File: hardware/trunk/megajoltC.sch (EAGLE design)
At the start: 92 parts, among them IC2 MCP1826, IC9 74AC240, U3 MAX9924, U4 ZXMS6004FF, U5 MAX9924, U6 ZXMS6004FF, U7 MCP1700, U8 FAN8303, X1 MINI_USB_SHIELD, X2 MOLEX_MINIFIT-22

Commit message: Schematic V1 for MJ2/C
Also added pinmux for xmc4200.  Board is partially routed to assist in pinout
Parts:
- removed C28: 1nF, rcl:C-USC0603
- removed C29: .001uf, rcl:C-USC0603
- removed C33: 10nF, rcl:C-USC0603
- removed C34: 0.1uF, rcl:C-USC0603
- removed C35: 1uF, rcl:C-USC0603
- removed C44: 0.22uf, rcl:C-USC0603
- removed C45: .1uf, rcl:C-USC0603
- removed C46: 10uF, rcl:CPOL-USSMCA
- removed C49: 0.1uf, rcl:C-USC0603
- removed D10, D11, D2, D3, D4, D5, D8, D9: schottky, smt_diodes:ZENER2
- removed IC9: 74AC240, 74xx-eu:74S240DW
- removed POWER, S1, S2: PANEL_LED, LEDs:PANEL_LED
- removed R21, R24, R25: 1K, rcl:R-US_R0603
- removed R33: 20K 1%, rcl:R-US_R0603
- removed R34: 39K 1%, rcl:R-US_R0603
- removed R37: 51K 1%, rcl:R-US_R0603
- removed R38: 10K 1%, rcl:R-US_R0603
- removed SV2: (no value), con-lsta:FE08-1
- removed U3, U5: MAX9924, max9924_9927:MAX9924
- removed U6: ZXMS6004FF, power_mosfets:ZXMS6004FF
- removed U7: MCP1700, mcp1700:MCP1700
- removed X2: MOLEX_MINIFIT-22, molex_mini-fit:MOLEX_MINIFIT-22
- added C10, C12: 10uF, resistor:C-USC0603
- added C11: 0.1uf, rcl:C-USC0603
- added C13, C15, C16, C17, C18, C19, C7, C8: 100nF, resistor:C-USC0603
- added C25, C26: 33pF, SparkFun:CAP0603
- added C3, C4: 47pF, resistor:C-USC0603
- added C48: 0.1uF, rcl:C-USC0805
- added C5: 100nf, resistor:C-USC0603
- added C6, C9: 4.7uF, resistor:C-USC0603
- added CN2: CAP_ARRAY_41206_ARRAY, cap_array:CAP_ARRAY_41206_ARRAY
- added IC1: IC_FT230X-SSOP-16, dp_devices:IC_FT230X-SSOP-16
- added IC3: MCP1826, linear:LM340S
- added J3: JUMPER_CLOSEDTHICK, jumpers:JUMPER_CLOSEDTHICK
- added L1: 1uH, smt_inductors:INDUCTOR
- added R1, R3: 27, resistor:R-US_R0603
- added R31: 100, resistor:R-US_R0603
- added R39: 1k, resistor:R-US_R0603
- added R4: 4.7k, resistor:R-US_R0603
- added R40, R41, R42: 100, rcl:R-US_R0603
- added R43, R44, R45, R46, R47: 1K, rcl:R-US_R0603
- added R5, R6: 10k, resistor:R-US_R0603
- added RN1: 5.6K, resistor-dil:4R-N0603-ARC
- added RN2: 10K, resistor-dil:4R-N0603-ARC
- added T2, T3: (no value), transistor:-NPN-SOT23-EBC
- added TC2: TC2050-IDC-NL, TagConnect:TC2050-IDC-NL
- added TLV271: TLV271, texas_instruments:TLV271
- added U$1: INF-PG-VQFN-48-53-5200X5200TE5, infineon_xmc:INF-PG-VQFN-48-53-5200X5200TE5
- added U$2: ESP8266_ESP-12, ESP8266-ESP12:ESP8266_ESP-12
- added U$3, U$7, U12: PESDXS4UD, smt_diodes:PESDXS4UD
- added U$4: 74AC240, dp_devices:74AC240
- added U$5: MAX9926, max9924_9927:MAX9926
- added U$6: TRIPLE_PANEL_LED, LEDs:TRIPLE_PANEL_LED
- added U1: MCP1700, mcp1700:MCP1700
- added U11: TLV274, op_amps:TLV274SO14
- added U18: MCP2551SO8, can:MCP2551SO8
- added X3: MOLEX_MINIFIT-22, molex_mini-fit:MOLEX_MINIFIT-22
- added XTAL1: 8MHz, SparkFun2:CRYSTAL5X3
- C20: value 1nF -> 10uF; device rcl:C-USC0603 -> rcl:CPOL-USSMCA
- C21: value .001uF -> 0.1uF; device rcl:C-USC0603 -> rcl:C-USC0603K
- C22: value 0.22uF -> 10nF
- C23: value 10nF -> 10uF; device rcl:C-USC0603 -> rcl:CPOL-USSMCA
- C24: value 0.1uF -> 10uF; device rcl:C-USC0603 -> rcl:CPOL-USSMCA
- C27: value 1uF -> .1uf; device rcl:C-USC0603 -> resistor:C-USC0603
- C30: value 0.22uf -> 0.1uF
- C31: value .001uf -> 1uF
- C32: value 0.22uf -> 1nF
- C43: value .001uf -> 1nF
- R10, R9: value 10K -> 100k; device rcl:R-US_R0603 -> resistor:R-US_R0603
- R11, R29, R30: value 100 -> 1K
- R12, R16, R19, R20: value 1K -> 10K; device rcl:R-US_R0603 -> rcl:R-US_R1206
- R14, R17: value 20K 1% -> 10K
- R15, R18: value 39K 1% -> 10K
- R22: value 1K -> 2.1k; device rcl:R-US_R0603 -> resistor:R-US_R0603
- R23: value 1K -> 10K
- R27: value 18K 1% -> 24K 1%
- R28: value 2.43K 1% -> 2.94K 1%
- R7: value 2.2K -> 120
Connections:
- removed net +12V: L2.2, R13.2, R25.2, R36.2, X2.P2
- removed net +6V: C2.+, IC2.IN
- removed net ADC0: C45.1, R37.2, R38.1
- removed net ADC4: C30.1, D8.A, D9.C, R14.2, R15.2
- removed net ADC5: C32.1, D10.A, D11.C, R17.2, R18.2
- removed net ADC6: C36.1, R32.2
- removed net ADC7: C44.1, D4.C, D5.A, R33.2, R34.2
- removed net AUX_IN: C29.1, R14.1, X2.P6
- removed net GPI0: D2.A, D3.C
- removed net GPO0: IC9B.A1
- removed net GPO1: IC9A.A4
- removed net GPO10: IC9A.G, IC9B.G
- removed net GPO11: U4.G
- removed net GPO2: IC9B.A2
- removed net GPO3: IC9A.A3
- removed net GPO4: IC9B.A3
- removed net GPO5: IC9A.A2
- removed net GPO6: IC9B.A4
- removed net GPO7: IC9A.A1
- removed net GPO8: R35.1
- removed net GPO9: U6.G
- removed net N$14: C20.2, R8.1, U5.IN-
- removed net N$19: R11.2, S1.A
- removed net N$6: C28.2, R10.1, U3.IN-
- removed net OPTION_IN: C21.1, R7.1, X2.P7
- removed net PROC_PULSE_IN: C22.1, R7.2
- removed net RESET: SV2.2
- removed net SAFE12V: C41.+, D6.C, D7.C, R37.1, U8.VIN
- removed net SHIFT_LIGHT: R25.1, U6.D1, X2.P20
- removed net TCK: SV2.5
- removed net TDI: SV2.3
- removed net TDO: SV2.6
- removed net TEMP_IN: C43.1, R33.1, X2.P4
- removed net TIMER0: U5.COUT
- removed net TIMER1: U3.COUT
- removed net TMS: SV2.4
- removed net V+: C46.+, SV2.1, U7.VOUT
- new net +3V3: C12.1, C13.1, C15.1, C16.1, C17.1, C18.1, C19.1, C20.+, C6.1, C7.1, C8.1, C9.1, IC1.VCC, R31.2, R6.2, R9.1, TC2.1, U$1.VBAT, U$1.VDDA, U$1.VDDC1, U$1.VDDC2, U$1.VDDP1, U$1.VDDP2, U$1.VDDP3, U$2.VCC, U1.VOUT
- new net AGND: C13.2, C27.2, C48.2, CN2A.1, CN2B.1, CN2D.1, J3.1, R22.1, RN2A.1, RN2B.1, RN2C.1, TLV271.GND, U$1.VSSA, U11G$5.V-, U12.2, U12.5
- new net ANALOG-FREQ_1_OPAMP_OUT1: RN1C.2, U11G$1.-IN, U11G$1.OUT
- new net ANALOG-FREQ_1_OPAMP_OUT2: RN1B.2, U11G$2.-IN, U11G$2.OUT
- new net ANALOG-FREQ_1_OPAMP_OUT3: RN1A.2, U11G$3.-IN, U11G$3.OUT
- new net ANALOG-FREQ_1_OPAMP_OUT4: RN1D.1, TLV271.IN-, TLV271.OUT
- new net CAM_TIM_IN: U$1.P2.4, U$5.COUT2
- new net CANH: R7.1, U18G$1.CANH, X3.P21
- new net CANL: R7.2, U18G$1.CANL, X3.P2
- new net CAN_RX: U$1.P14.3, U18G$1.RXD
- new net CAN_TX: U$1.P2.0, U18G$1.TXD
- new net CLT_ADC: RN1C.1, RN2C.2, U$1.P14.0
- new net CLT_IN: R12.2, X3.P11
- new net CRANK_TIM_IN: U$1.P1.3, U$5.COUT1
- new net ESP_GPIO0: U$2.GPIO0
- new net ESP_RXD: U$1.P2.5, U$2.RXD
- new net ESP_TXD: U$1.P2.2, U$2.TXD
- new net FTDI_DM: C3.1, R1.1, X1G$1.2
- new net FTDI_DP: C4.1, R3.1, X1G$1.3
- new net FTDI_RXD: IC1.RXD, U$1.P1.5
- new net FTDI_TXD: IC1.TXD, U$1.P1.4
- new net FTDI_VBUS_SENSE: IC1.CBUS0, R4.1, R5.2
- new net GPO_COIL1: U$1.P0.0, U$4G$1.A1
- new net GPO_COIL2: U$1.P0.1, U$4G$1.A2
- new net GPO_COIL3: U$1.P0.2, U$4G$1.A3
- new net GPO_COIL4: U$1.P0.3, U$4G$1.A4
- new net GPO_COIL5: U$1.P0.4, U$4G$2.A1
- new net GPO_COIL6: U$1.P0.5, U$4G$2.A2
- new net GPO_COIL7: U$1.P0.6, U$4G$2.A3
- new net GPO_COIL8: U$1.P0.7, U$4G$2.A4
- new net GPO_COIL_EN: U$1.P0.8, U$4G$1.G, U$4G$2.G
- new net IAT_ADC: RN1A.1, RN2A.2, U$1.P14.4
- new net IAT_IN: R19.2, X3.P12
- new net MAP_ADC: C36.1, R32.2, U$1.P14.7
- new net MAX_DIRN: R14.1, U$5.DIRN
- new net N$1: IC1.USB+, R3.2
- new net N$17: C10.1, R6.1, U$2.REST
- new net N$18: R31.1, U$2.CH_PD
- new net N$20: R40.2, U$6G$1.A
- new net N$23: R42.2, U$6G$3.A
- new net N$24: R39.2, U$2.GPIO15
- new net N$25: C25.2, U$1.XTAL1, XTAL1.2
- new net N$36: R11.1, U$3.6, U$4G$1.Y1
- new net N$37: R29.1, U$3.4, U$4G$1.Y2
- new net N$38: R30.1, U$3.3, U$4G$1.Y3
- new net N$39: R43.1, U$3.1, U$4G$1.Y4
- new net N$4: C5.1, IC1.!RESET, IC1.3V3OUT, IC1.VCCIO
- new net N$40: R44.1, U$4G$2.Y1, U$7.6
- new net N$41: R45.1, U$4G$2.Y2, U$7.4
- new net N$42: R46.1, U$4G$2.Y3, U$7.3
- new net N$43: R47.1, U$4G$2.Y4, U$7.1
- new net N$56: C23.+, IC3.OUT, L1.1
- new net PGM_GPO: U$1.P2.3, U4.G
- new net RAW_+12V: L2.2, X3.P22
- new net SAFE_+12V: C27.1, C41.+, D6.C, D7.C, R13.2, R20.2, R36.2, TLV271.VDD, U8.VIN
- new net STATUS_LED_1: R2.2, U$1.P14.8
- new net STATUS_LED_2: R8.2, U$1.P14.9
- new net SWCLK: R10.2, TC2.4, U$1.TCK/SWCLK
- new net SWDIO: R9.2, TC2.2, U$1.TMS/SWDIO
- new net TACH_GPO: R35.1, U$1.P2.1
- new net TPS_ADC: RN1B.1, RN2B.2, U$1.P14.5
- new net VBATT_ADC: R22.2, RN1D.2, U$1.P14.6
- new net VDD: C2.+, C24.+, C39.+, IC2.IN, IC3.IN, L3.1, R27.1, U1.VIN
- new net XMC_RESET: TC2.10, U$1.PORST
- net +5V: now also C11.1, C21.1, C22.1, C30.1, C31.1, L1.2, R14.2, R40.1, R41.1, R42.1, U$4G$3.V+, U$5.VCC, U11G$5.V+, U18G$2.VCC; no longer C23.1, C24.1, C27.1, C33.1, C34.1, C35.1, C39.+, C49.1, D10.C, D2.C, D5.C, D8.C, IC9P.VCC, L3.1, R11.1, R27.1, R30.1, U3.VCC, U5.VCC, U7.VIN
- net CAM_VRS+: now also R17.2, X3.P14; no longer R9.2, X2.P9
- net CAM_VRS-: now also R15.2, X3.P9; no longer R10.2, X2.P8
- net COIL1: now also R11.2, X3.P20; no longer R12.2, X2.P12
- net COIL2: now also R29.2, X3.P3; no longer R16.2, X2.P13
- net COIL3: now also R30.2, X3.P19; no longer R19.2, X2.P14
- net COIL4: now also R43.2, X3.P4; no longer R20.2, X2.P15
- net COIL5: now also R44.2, X3.P18; no longer R21.2, X2.P16
- net COIL6: now also R45.2, X3.P5; no longer R22.2, X2.P17
- net COIL7: now also R46.2, X3.P17; no longer R23.2, X2.P18
- net COIL8: now also R47.2, X3.P6; no longer R24.2, X2.P19
- net CRANK_VRS+: now also R18.2, X3.P15; no longer R2.2, X2.P11
- net CRANK_VRS-: now also R23.2, X3.P8; no longer R8.2, X2.P10
- net GND: now also C10.2, C11.2, C12.2, C15.2, C16.2, C17.2, C18.2, C19.2, C20.-, C23.-, C24.-, C25.1, C26.1, C3.2, C4.2, C5.2, C6.2, C7.2, C8.2, C9.2, IC1.GND@1, IC1.GND@2, IC3.GND@1, IC3.GND@2, J3.2, R10.1, R39.1, R5.1, T2.E, T3.E, TC2.3, U$1.VSS, U$1.VSS_PAD, U$2.GND, U$3.2, U$3.5, U$4G$3.GND, U$5.BIAS1, U$5.BIAS2, U$5.GND, U$5.INT_THRS1, U$5.INT_THRS2, U$5.ZERO_EN, U$6G$1.C, U$7.2, U$7.5, U1.GND, U18G$1.RS, U18G$2.GND, X3.P1; no longer C23.2, C24.2, C27.2, C29.2, C32.2, C33.2, C34.2, C35.2, C43.2, C44.2, C45.2, C46.-, C49.2, D11.A, D3.A, D4.A, D9.A, IC9P.GND, R15.1, R18.1, R29.2, R34.1, R38.2, SV2.7, SV2.8, U3.BIAS, U3.GND, U3.INT_THRS, U3.ZERO_EN, U5.BIAS, U5.GND, U5.INT_THRS, U5.ZERO_EN, U6.S1, U7.GND, X2.P1
- net N$2: now also T2.B; no longer C20.1, U5.IN+
- net N$21: now also C26.2, U$1.XTAL2, XTAL1.1; no longer R30.2, S2.A
- net N$22: now also R41.2, U$6G$2.A; no longer POWER.C, R29.1
- net N$26: now also CN2B.2, U11G$1.+IN, U12.1; no longer IC9B.Y1
- net N$27: now also C43.1, R18.1, U$5.IN1+; no longer IC9A.Y4, R16.1
- net N$28: now also CN2A.2, R16.1, U11G$2.+IN, U12.6; no longer IC9B.Y2, R19.1
- net N$29: now also C32.1, R15.1, U$5.IN2-; no longer IC9A.Y3, R20.1
- net N$3: now also IC1.USB-, R1.2; no longer X1G$1.3
- net N$30: now also CN2D.2, R19.1, U11G$3.+IN, U12.4; no longer IC9B.Y3, R21.1
- net N$31: now also C48.1, R20.1, TLV271.IN+, U12.3; no longer IC9A.Y2, R22.1
- net N$32: now also C32.2, R17.1, U$5.IN2+; no longer IC9B.Y4, R23.1
- net N$33: now also C43.2, R23.1, U$5.IN1-; no longer IC9A.Y1, R24.1
- net N$5: now also R8.1, T3.B; no longer C28.1, R9.1, U3.IN+
- net PGM_OUT: now also X3.P16; no longer X2.P21
- net PROC_STATUS_LED_OUT1: now also T2.C, U$6G$2.C; no longer S1.C
- net PROC_STATUS_LED_OUT2: now also T3.C, U$6G$3.C; no longer S2.C
- net TACH_OUT: now also X3.P7; no longer X2.P22
- net TPS_IN: now also R16.2, X3.P10; no longer C31.1, R17.1, X2.P5
- net VBUS: now also R4.2
- net VREF: now also X3.P13; no longer X2.P3
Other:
- note added: "Analog Buffers"
- note added: "XMC4200 PS Decoupling"

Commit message: Schematic, second draft complete
Also added gitignore
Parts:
- removed C27: .1uf, resistor:C-USC0603
- removed C48: 0.1uF, rcl:C-USC0805
- removed L4: 1uH, smt_inductors:INDUCTOR
- removed R20: 10K, rcl:R-US_R1206
- removed R22: 2.1k, resistor:R-US_R0603
- removed T2, T3: (no value), transistor:-NPN-SOT23-EBC
- removed TLV271: TLV271, texas_instruments:TLV271
- removed X3: MOLEX_MINIFIT-22, molex_mini-fit:MOLEX_MINIFIT-22
- added C28: .1uf, resistor:C-USC0603
- added C45: .1uf, rcl:C-USC0603
- added D2: (no value), diode:SCHOTTKY-DIODESMC
- added D4: PESD1CAN, diode:PESD1CAN
- added R21, R24: 10k, resistor:R-US_R0603
- added R37: 43K 1%, rcl:R-US_R0603
- added R38: 10K 1%, rcl:R-US_R0603
- added U$8: 24LC64-I/SN, element14_microchip:24LC64-I/SN
- added U$9: XMC4200F64K256QFP64, infineon_xmc:XMC4200F64K256QFP64
- R2: device rcl:R-US_R0603 -> rcl:R-US_R1206
- R28: value 2.94K 1% -> 2.7K 1%
- R32: value 270 -> 5.6k
- R8: value 10K -> 10k
- U$1: value INF-PG-VQFN-48-53-5200X5200TE5 -> MOLEX_MINIFIT-JR-24; device infineon_xmc:INF-PG-VQFN-48-53-5200X5200TE5 -> molex_mini-fit:MOLEX_MINIFIT-JR-24
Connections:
- removed net ANALOG-FREQ_1_OPAMP_OUT4: RN1D.1, TLV271.IN-, TLV271.OUT
- removed net N$5: R8.1, T3.B
- removed net N$53: C1.+, IC2.OUT, L4.1
- removed net N$56: C23.+, IC3.OUT, L1.1
- removed net PROC_STATUS_LED_OUT1: T2.C, U$6G$2.C
- removed net PROC_STATUS_LED_OUT2: T3.C, U$6G$3.C
- new net AUX_ADC: RN1D.1, RN2D.2, U$9.P14.3
- new net AUX_IN: R2.2, U$1.P14
- new net EEPROM_SCL: R24.1, U$8.SCL, U$9.P0.11
- new net EEPROM_SDA: R21.1, U$8.SDA, U$9.P0.4
- new net N$14: RN1D.2, U11G$4.-IN, U11G$4.OUT
- new net UNUSED: U$1.P10
- new net VCC: C1.+, IC2.OUT, R31.2, R6.2, U$2.VCC
- net +3V3: now also C28.1, R21.2, R24.2, R40.1, R41.1, R42.1, U$8.VCC, U$9.VBAT, U$9.VDDA, U$9.VDDC1, U$9.VDDC2, U$9.VDDP1, U$9.VDDP2, U$9.VDDP3; no longer R31.2, R6.2, U$1.VBAT, U$1.VDDA, U$1.VDDC1, U$1.VDDC2, U$1.VDDP1, U$1.VDDP2, U$1.VDDP3, U$2.VCC
- net +5V: now also C23.+, IC3.OUT, L1.1; no longer L1.2, R40.1, R41.1, R42.1
- net AGND: now also C45.2, CN2C.2, R38.2, RN2D.1, U$9.VSSA; no longer C27.2, C48.2, R22.1, TLV271.GND, U$1.VSSA
- net CAM_TIM_IN: now also U$9.P2.4; no longer U$1.P2.4
- net CAM_VRS+: now also U$1.P16; no longer X3.P14
- net CAM_VRS-: now also U$1.P9; no longer X3.P9
- net CANH: now also D4.2, U$1.P23; no longer X3.P21
- net CANL: now also D4.1, U$1.P2; no longer X3.P2
- net CAN_RX: now also U$9.P2.6; no longer U$1.P14.3
- net CAN_TX: now also U$9.P2.0, U$9.P2.7; no longer U$1.P2.0
- net CLT_ADC: now also U$9.P14.0; no longer U$1.P14.0
- net CLT_IN: now also U$1.P12; no longer X3.P11
- net COIL1: now also U$1.P22; no longer X3.P20
- net COIL2: now also U$1.P3; no longer X3.P3
- net COIL3: now also U$1.P21; no longer X3.P19
- net COIL4: now also U$1.P4; no longer X3.P4
- net COIL5: now also U$1.P20; no longer X3.P18
- net COIL6: now also U$1.P5; no longer X3.P5
- net COIL7: now also U$1.P19; no longer X3.P17
- net COIL8: now also U$1.P6; no longer X3.P6
- net CRANK_TIM_IN: now also U$9.P2.8; no longer U$1.P1.3
- net CRANK_VRS+: now also U$1.P17; no longer X3.P15
- net CRANK_VRS-: now also U$1.P8; no longer X3.P8
- net ESP_GPIO0: now also U$9.P1.3
- net ESP_RXD: now also U$9.P2.5; no longer U$1.P2.5
- net ESP_TXD: now also U$9.P2.2; no longer U$1.P2.2
- net FTDI_RXD: now also U$9.P1.5; no longer U$1.P1.5
- net FTDI_TXD: now also U$9.P1.4; no longer U$1.P1.4
- net GND: now also C28.2, D4.3, R8.1, U$1.P1, U$8.A0, U$8.A1, U$8.A2, U$8.VSS, U$9.VSS, U$9.VSS0, U$9.VSS_PAD; no longer T2.E, T3.E, U$1.VSS, U$1.VSS_PAD, X3.P1
- net GPO_COIL1: now also U$9.P0.0; no longer U$1.P0.0
- net GPO_COIL2: now also U$9.P0.1; no longer U$1.P0.1
- net GPO_COIL3: now also U$9.P0.2; no longer U$1.P0.2
- net GPO_COIL4: now also U$9.P0.3; no longer U$1.P0.3
- net GPO_COIL5: now also U$9.P0.5; no longer U$1.P0.4
- net GPO_COIL6: now also U$9.P0.6; no longer U$1.P0.5
- net GPO_COIL7: now also U$9.P0.7; no longer U$1.P0.6
- net GPO_COIL8: now also U$9.P0.8; no longer U$1.P0.7
- net GPO_COIL_EN: now also U$9.P0.9; no longer U$1.P0.8
- net IAT_ADC: now also U$9.P14.4; no longer U$1.P14.4
- net IAT_IN: now also U$1.P13; no longer X3.P12
- net MAP_ADC: now also R8.2, U$9.P14.7; no longer U$1.P14.7
- net N$2: now also D2.A, L1.2; no longer R2.1, T2.B
- net N$21: now also U$9.XTAL2; no longer U$1.XTAL2
- net N$25: now also U$9.XTAL1; no longer U$1.XTAL1
- net N$31: now also CN2C.1, R2.1, U11G$4.+IN; no longer C48.1, R20.1, TLV271.IN+
- net PGM_GPO: now also U$9.P2.3; no longer U$1.P2.3
- net PGM_OUT: now also U$1.P18; no longer X3.P16
- net RAW_+12V: now also U$1.P24; no longer X3.P22
- net SAFE_+12V: now also R37.1; no longer C27.1, R20.2, TLV271.VDD
- net STATUS_LED_1: now also U$6G$2.C, U$9.P2.9; no longer R2.2, U$1.P14.8
- net STATUS_LED_2: now also U$6G$3.C, U$9.P2.14; no longer R8.2, U$1.P14.9
- net SWCLK: now also U$9.TCK/SWCLK; no longer U$1.TCK/SWCLK
- net SWDIO: now also U$9.TMS/SWDIO; no longer U$1.TMS/SWDIO
- net TACH_GPO: now also U$9.P2.1; no longer U$1.P2.1
- net TACH_OUT: now also U$1.P7; no longer X3.P7
- net TPS_ADC: now also U$9.P14.5; no longer U$1.P14.5
- net TPS_IN: now also U$1.P11; no longer X3.P10
- net VBATT_ADC: now also C45.1, R37.2, R38.1, U$9.P14.6; no longer R22.2, RN1D.2, U$1.P14.6
- net VREF: now also D2.C, U$1.P15; no longer L4.2, X3.P13
- net XMC_RESET: now also U$9.PORST; no longer U$1.PORST
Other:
- note added: "1A 3v3 Supply for ESP-12"
- note added: "1A 5v supply for 5v buffers. Additional filtering for VREF"
- note added: "250mA 3v3 supply for digital logic (MCU)"
- moved on the sheet: C1, C2, C25, C26, C36, IC2, R32, R8, RN1D, XTAL1

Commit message: Board routed. V1
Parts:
- D2: value (none) -> SCHOTTKY; device diode:SCHOTTKY-DIODESMC -> smt_diodes:SCHOTTKY
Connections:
- new net ESP_GPIO2: U$2.GPIO2, U$9.P1.3
- net CAN_TX: no longer U$9.P2.0
- net ESP_GPIO0: now also U$9.P1.2; no longer U$9.P1.3
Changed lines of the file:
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@@
 <setting verticaltext="up"/>
 </settings>
-<grid distance="0.1" unitdist="inch" unit="inch" style="lines" multiple="1" display="yes" altdistance="0.01" altunitdist="inch" altunit="inch"/>
+<grid distance="0.1" unitdist="inch" unit="inch" style="lines" multiple="1" display="no" altdistance="0.01" altunitdist="inch" altunit="inch"/>
 <layers>
 <layer number="1" name="Top" color="12" fill="1" visible="no" active="no"/>
@@
 <part name="P+4" library="supply1" deviceset="+5V" device=""/>
 <part name="P+7" library="supply2" deviceset="V+" device="" value="VREF"/>
-<part name="D2" library="diode" deviceset="SCHOTTKY-DIODE" device="SMC"/>
 <part name="C1" library="rcl" deviceset="CPOL-US" device="SMCA" value="10uF"/>
 <part name="GND12" library="supply1" deviceset="GND" device=""/>
@@
 <part name="GND19" library="supply1" deviceset="GND" device=""/>
 <part name="R8" library="rcl" deviceset="R-US_" device="R0603" value="10k"/>
+<part name="D2" library="smt_diodes" deviceset="SCHOTTKY" device=""/>
 </parts>
 <sheets>
@@
 </segment>
 <segment>
-<pinref part="U$9" gate="G$1" pin="P1.3"/>
-<wire x1="-134.62" y1="129.54" x2="-132.08" y2="129.54" width="0.1524" layer="91"/>
-<label x="-132.08" y="129.54" size="0.8128" layer="95" xref="yes"/>
+<pinref part="U$9" gate="G$1" pin="P1.2"/>
+<wire x1="-134.62" y1="132.08" x2="-132.08" y2="132.08" width="0.1524" layer="91"/>
+<label x="-132.08" y="132.08" size="0.8128" layer="95" xref="yes"/>
 </segment>
 </net>
@@
 </net>
 <net name="CAN_TX" class="0">
-<segment>
-<pinref part="U$9" gate="G$1" pin="P2.0"/>
-<wire x1="-200.66" y1="170.18" x2="-203.2" y2="170.18" width="0.1524" layer="91"/>
-<label x="-203.2" y="170.18" size="0.8128" layer="95" rot="R180" xref="yes"/>
-</segment>
 <segment>
 <pinref part="U$9" gate="G$1" pin="P2.7"/>
@@
 <wire x1="-200.66" y1="149.86" x2="-203.2" y2="149.86" width="0.1524" layer="91"/>
 <label x="-203.2" y="149.86" size="0.8128" layer="95" rot="R180" xref="yes"/>
+</segment>
+</net>
+<net name="ESP_GPIO2" class="0">
+<segment>
+<pinref part="U$2" gate="G$1" pin="GPIO2"/>
+<wire x1="-233.68" y1="223.52" x2="-231.14" y2="223.52" width="0.1524" layer="91"/>
+<label x="-231.14" y="223.52" size="0.8128" layer="95" xref="yes"/>
+</segment>
+<segment>
+<pinref part="U$9" gate="G$1" pin="P1.3"/>
+<wire x1="-134.62" y1="129.54" x2="-132.08" y2="129.54" width="0.1524" layer="91"/>
+<label x="-132.08" y="129.54" size="0.8128" layer="95" xref="yes"/>
 </segment>
 </net>
@@
 <instance part="P+4" gate="1" x="304.8" y="160.02"/>
 <instance part="P+7" gate="1" x="335.28" y="160.02"/>
-<instance part="D2" gate="G$1" x="327.66" y="147.32"/>
 <instance part="C1" gate="G$1" x="248.92" y="185.42" smashed="yes">
 <attribute name="NAME" x="249.936" y="186.055" size="1.778" layer="95"/>
@@
 <instance part="VDD3" gate="G$1" x="208.28" y="200.66"/>
 <instance part="P+3" gate="VCC" x="248.92" y="205.74"/>
+<instance part="D2" gate="G$1" x="327.66" y="147.32" smashed="yes">
+<attribute name="NAME" x="327.5584" y="151.9936" size="1.778" layer="95" rot="R90"/>
+</instance>
 </instances>
 <busses>
@@
 <net name="VREF" class="0">
 <segment>
-<pinref part="D2" gate="G$1" pin="C"/>
 <pinref part="P+7" gate="1" pin="V+"/>
 <wire x1="330.2" y1="147.32" x2="335.28" y2="147.32" width="0.1524" layer="91"/>
 <wire x1="335.28" y1="147.32" x2="335.28" y2="157.48" width="0.1524" layer="91"/>
-</segment>
-</net>
+<pinref part="D2" gate="G$1" pin="C"/>
+</segment>
+</net>

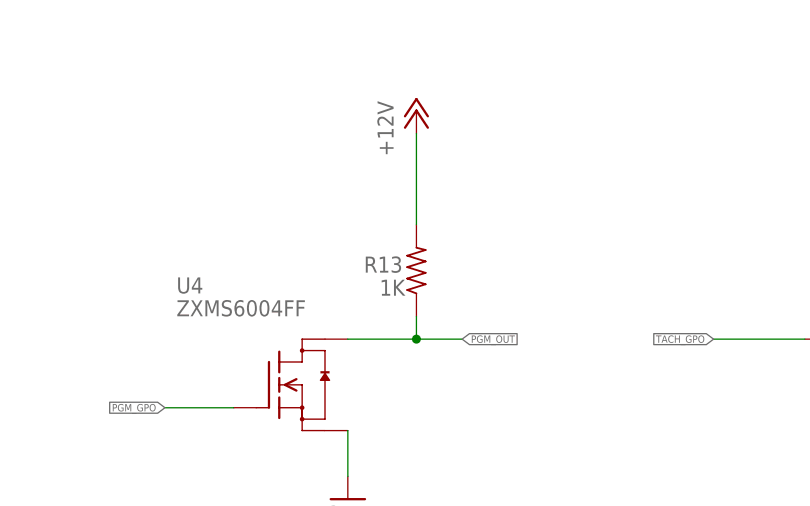
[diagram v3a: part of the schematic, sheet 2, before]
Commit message: Remove R13, minor ground pour changes
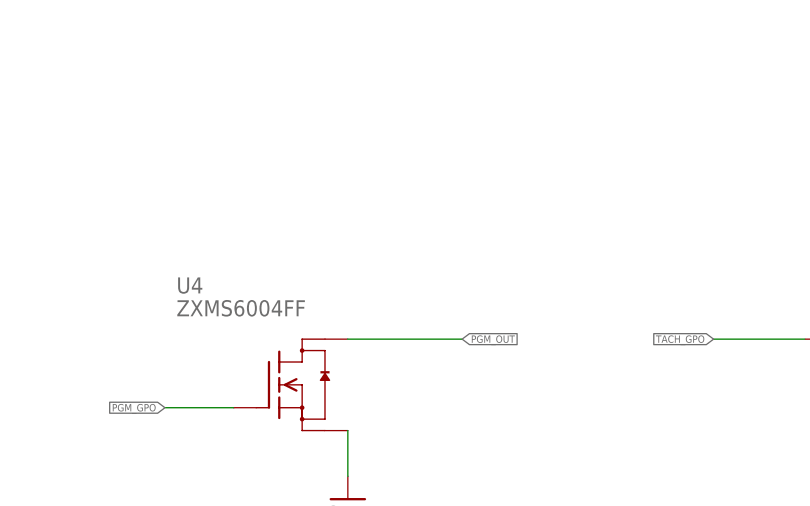
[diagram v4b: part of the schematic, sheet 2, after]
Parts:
- removed R13: 1K, rcl:R-US_R0603
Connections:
- net PGM_OUT: no longer R13.1
- net SAFE_+12V: no longer R13.2
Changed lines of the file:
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@@
 <part name="X1" library="cnkls_parts" deviceset="MINI_USB_SHIELD" device=""/>
 <part name="FRAME1" library="frames" deviceset="FRAME_B_L" device=""/>
-<part name="R13" library="rcl" deviceset="R-US_" device="R0603" value="1K"/>
 <part name="U4" library="power_mosfets" deviceset="ZXMS6004FF" device=""/>
 <part name="GND5" library="supply1" deviceset="GND" device=""/>
@@
 <part name="RN2" library="resistor-dil" deviceset="4R-N" device="0603-ARC" value="10K"/>
 <part name="CN2" library="cap_array" deviceset="CAP_ARRAY_4" device="1206_ARRAY" value=""/>
-<part name="P+6" library="supply1" deviceset="+12V" device=""/>
 <part name="P+8" library="supply1" deviceset="+12V" device=""/>
 <part name="U18" library="can" deviceset="MCP2551" device="SO8"/>
@@
 </plain>
 <instances>
-<instance part="R13" gate="G$1" x="-22.86" y="101.6" smashed="yes" rot="R90">
-<attribute name="NAME" x="-24.384" y="103.1494" size="1.778" layer="95" rot="R180"/>
-<attribute name="VALUE" x="-24.13" y="100.584" size="1.778" layer="96" rot="R180"/>
-</instance>
 <instance part="U4" gate="G$1" x="-38.1" y="88.9" smashed="yes">
 <attribute name="NAME" x="-49.53" y="99.06" size="1.778" layer="95"/>
@@
 <attribute name="VALUE" x="-129.54" y="104.14" size="1.778" layer="96"/>
 </instance>
-<instance part="P+6" gate="1" x="-22.86" y="119.38"/>
 <instance part="P+8" gate="1" x="38.1" y="119.38"/>
 <instance part="U$6" gate="G$1" x="-137.16" y="111.76" rot="R90"/>
@@
 <net name="PGM_OUT" class="0">
 <segment>
-<wire x1="-30.48" y1="93.98" x2="-22.86" y2="93.98" width="0.1524" layer="91"/>
-<wire x1="-22.86" y1="96.52" x2="-22.86" y2="93.98" width="0.1524" layer="91"/>
-<wire x1="-22.86" y1="93.98" x2="-17.78" y2="93.98" width="0.1524" layer="91"/>
-<junction x="-22.86" y="93.98"/>
-<pinref part="R13" gate="G$1" pin="1"/>
+<wire x1="-30.48" y1="93.98" x2="-17.78" y2="93.98" width="0.1524" layer="91"/>
 <pinref part="U4" gate="G$1" pin="D1"/>
 <label x="-17.78" y="93.98" size="0.8128" layer="95" xref="yes"/>
@@
 <net name="SAFE_+12V" class="0">
 <segment>
-<pinref part="R13" gate="G$1" pin="2"/>
-<pinref part="P+6" gate="1" pin="+12V"/>
-<wire x1="-22.86" y1="106.68" x2="-22.86" y2="116.84" width="0.1524" layer="91"/>
-</segment>
-<segment>
 <pinref part="R36" gate="G$1" pin="2"/>
